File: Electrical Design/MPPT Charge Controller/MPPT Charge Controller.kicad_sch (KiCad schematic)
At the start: 0 parts

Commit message: Created BQ24650 symbol and footprint
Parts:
- added U1: ~, MPPT Charge Controller Footprint Library:VQFN-16_EP_3.5x3.5_Pitch0.5mm, symbol MPPT Charge Controller Symbol Library:BQ24650
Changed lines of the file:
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@@
 	(generator_version "8.0")
 	(paper "A4")
+	(symbol
+		(lib_id "MPPT Charge Controller Symbol Library:BQ24650")
+		(at 96.52 81.28 0)
+		(unit 1)
+		(exclude_from_sim no)
+		(in_bom yes)
+		(on_board yes)
+		(dnp no)
+		(fields_autoplaced yes)
+		(property "Reference" "U1"
+			(at 96.52 57.15 0)
+			(effects
+				(font
+					(size 1.27 1.27)
+				)
+			)
+		)
+		(property "Value" "~"
+			(at 96.52 59.69 0)
+			(effects
+				(font
+					(size 1.27 1.27)
+				)
+			)
+		)
+		(property "Footprint" "MPPT Charge Controller Footprint Library:VQFN-16_EP_3.5x3.5_Pitch0.5mm"
+			(at 96.52 58.928 0)
+			(effects
+				(font
+					(size 1.27 1.27)
+				)
+				(hide yes)
+			)
+		)
+		(property "Datasheet" ""
+			(at 96.52 81.28 0)
+			(effects
+				(font
+					(size 1.27 1.27)
+				)
+				(hide yes)
+			)
+		)
+		(property "Description" ""
+			(at 96.52 81.28 0)
+			(effects
+				(font
+					(size 1.27 1.27)
+				)
+				(hide yes)
+			)
+		)
+		(pin "14"
+		)
+		(pin "11"
+		)
+		(pin "8"
+		)
+		(pin "13"
+		)
+		(pin "1"
+		)
+		(pin "10"
+		)
+		(pin "12"
+		)
+		(pin "16"
+		)
+		(pin "2"
+		)
+		(pin "15"
+		)
+		(pin "3"
+		)
+		(pin "4"
+		)
+		(pin "5"
+		)
+		(pin "6"
+		)
+		(pin "7"
+		)
+		(pin "9"
+		)
+		(instances
+			(project "MPPT Charge Controller"
+				(path "/6fccb5b0-46ff-4014-9169-aa61e4064f3f"
+					(reference "U1")
+					(unit 1)
+				)
+			)
+		)
+	)
 	(sheet_instances
 		(path "/"

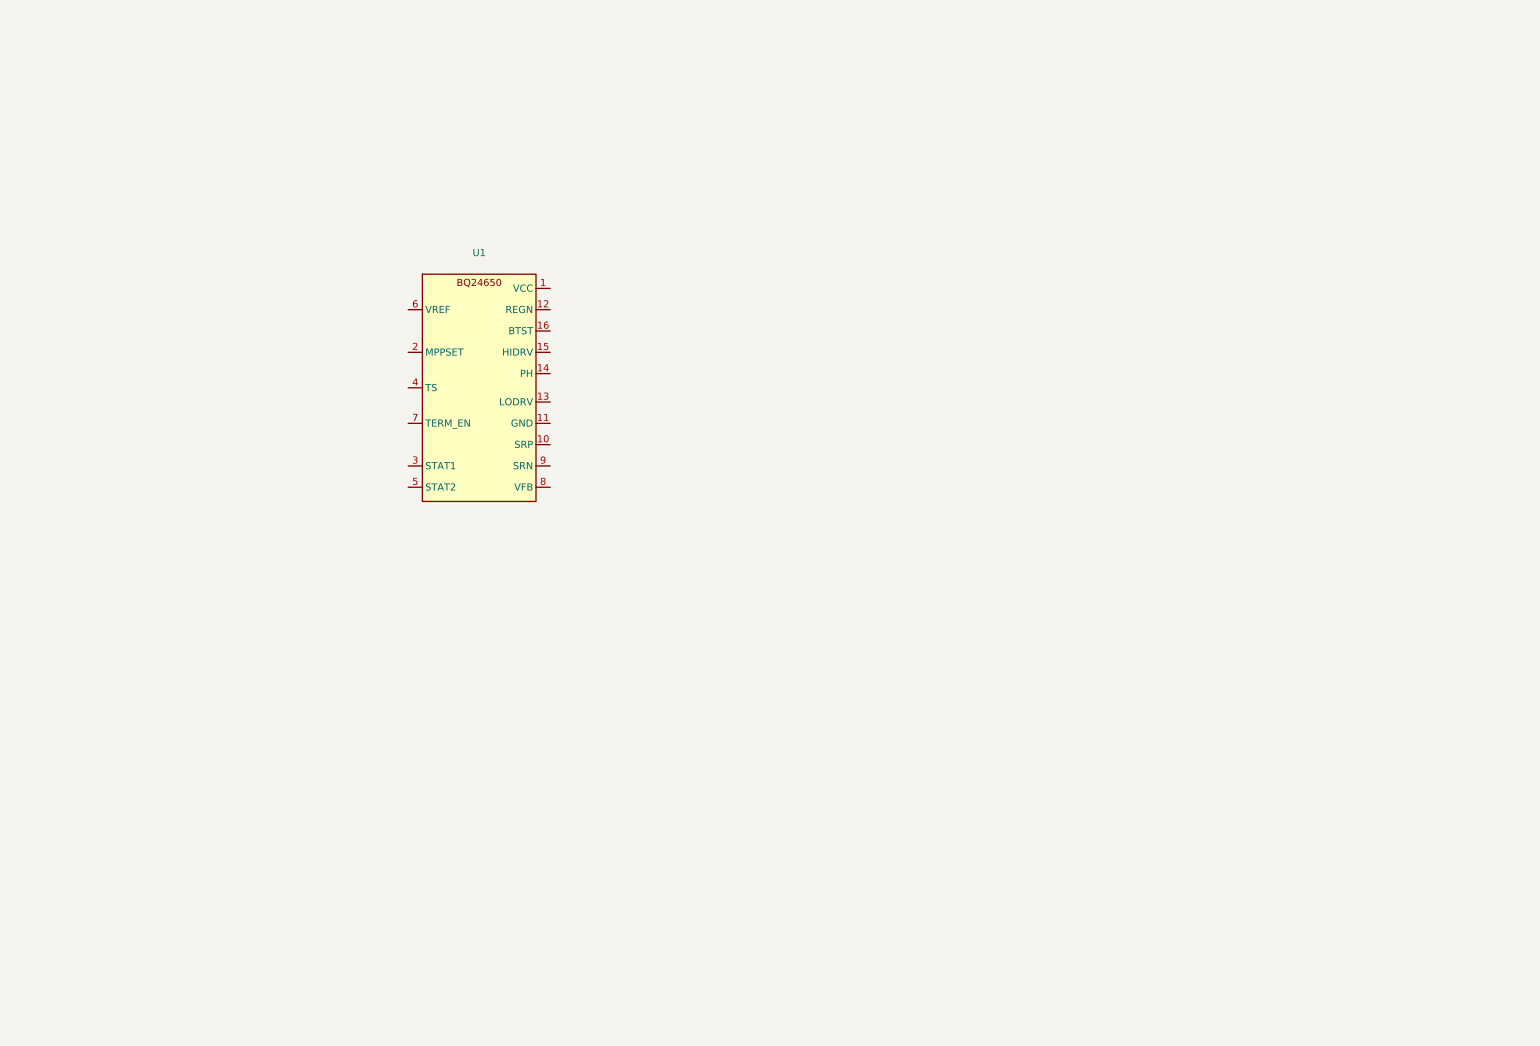
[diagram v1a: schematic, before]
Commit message: Added circuitry to schematic
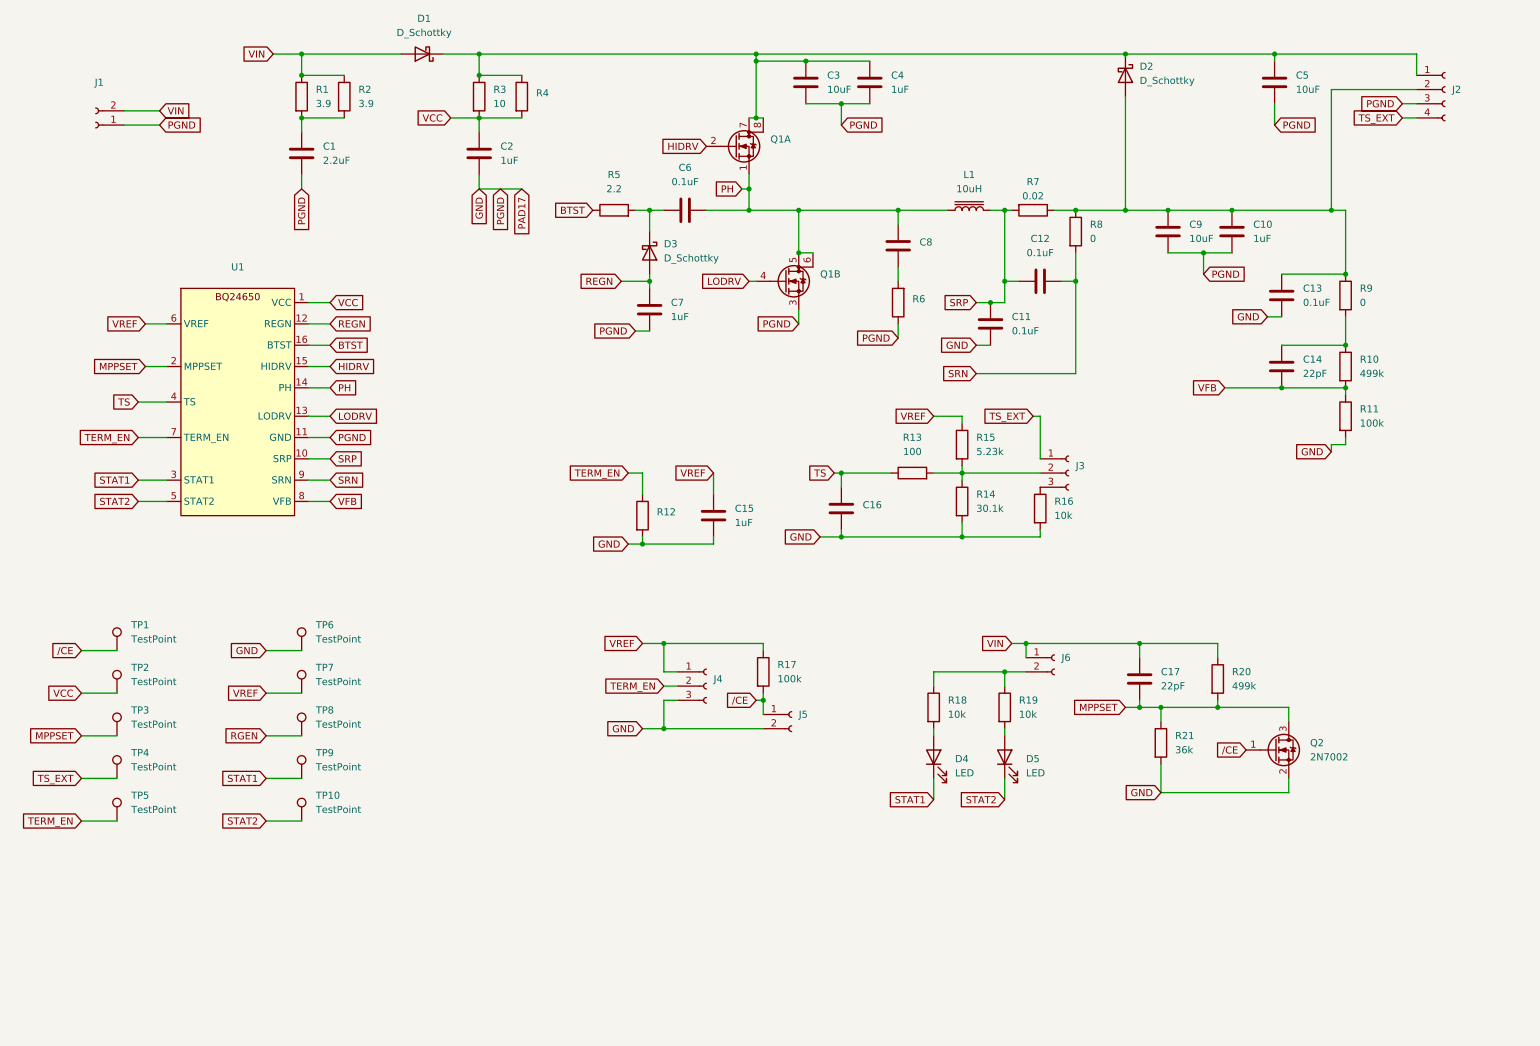
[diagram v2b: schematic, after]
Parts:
- added C1: 2.2uF, symbol Device:C
- added C10, C15, C2, C4, C7: 1uF, symbol Device:C
- added C11, C12, C13, C6: 0.1uF, symbol Device:C
- added C14, C17: 22pF, symbol Device:C
- added C16, C8: ~, symbol Device:C
- added C3, C5, C9: 10uF, symbol Device:C
- added D1, D2, D3: D_Schottky, symbol Device:D_Schottky
- added D4, D5: LED, symbol Device:LED
- added J1, J5, J6: Conn_01x02_Socket, symbol Connector:Conn_01x02_Socket
- added J2: Conn_01x04_Socket, symbol Connector:Conn_01x04_Socket
- added J3, J4: Conn_01x03_Socket, symbol Connector:Conn_01x03_Socket
- added L1: 10uH, symbol Device:L_Iron
- added Q1: Q_Dual_NMOS_S1G1S2G2D2D2D1D1, symbol Device:Q_Dual_NMOS_S1G1S2G2D2D2D1D1
- added Q2: 2N7002, Package_TO_SOT_SMD:SOT-23, symbol Transistor_FET:2N7002
- added R1, R2: 3.9, symbol Device:R
- added R10, R20: 499k, symbol Device:R
- added R11, R17: 100k, symbol Device:R
- added R12, R4, R6: ~, symbol Device:R
- added R13: 100, symbol Device:R
- added R14: 30.1k, symbol Device:R
- added R15: 5.23k, symbol Device:R
- added R16, R18, R19: 10k, symbol Device:R
- added R21: 36k, symbol Device:R
- added R3: 10, symbol Device:R
- added R5: 2.2, symbol Device:R
- added R7: 0.02, symbol Device:R
- added R8, R9: 0, symbol Device:R
- added TP1, TP10, TP2, TP3, TP4, TP5, TP6, TP7, TP8, TP9: TestPoint, symbol Connector:TestPoint
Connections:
- net VCC: now reaches U1.1 (VCC)
- net VCC: now also C2.1, R3.2, R4.2, TP2.1
- net SRP: now reaches U1.10 (SRP)
- net SRP: now also C11.2, C12.2, L1.2, R7.2
- net GND: now reaches U1.11 (GND)
- net GND: now also C1.2, C10.2, C11.1, C13.1, C15.2, C16.2, C2.2, C3.2, C4.2, C5.2, C7.1, C9.2, J1.1 (Pin_1), J2.3 (Pin_3), J4.3 (Pin_3), J5.2 (Pin_2), Q1.3 (S), Q2.2 (S), R11.2, R12.2, R14.2, R16.2, R21.2, R6.1, TP6.1
- net REGN: now reaches U1.12 (REGN)
- net REGN: now also C7.2, D3.2 (A)
- net LODRV: now reaches U1.13 (LODRV)
- net LODRV: now also Q1.4 (G)
- net PH: now reaches U1.14 (PH)
- net PH: now also C6.2, C8.1, L1.1, Q1.1 (S), Q1.5 (D), Q1.6 (D)
- net HIDRV: now reaches U1.15 (HIDRV)
- net HIDRV: now also Q1.2 (G)
- net BTST: now reaches U1.16 (BTST)
- net BTST: now also R5.1
- net MPPSET: now reaches U1.2 (MPPSET)
- net MPPSET: now also C17.2, Q2.3 (D), R20.2, R21.1, TP3.1
- net STAT1: now reaches U1.3 (STAT1)
- net STAT1: now also D4.1 (K), TP9.1
- net TS: now reaches U1.4 (TS)
- net TS: now also C16.1, R13.1
- net STAT2: now reaches U1.5 (STAT2)
- net STAT2: now also D5.1 (K), TP10.1
- net VREF: now reaches U1.6 (VREF)
- net VREF: now also C15.1, J4.1 (Pin_1), R15.1, R17.1, TP7.1
- net TERM_EN: now reaches U1.7 (TERM_EN)
- net TERM_EN: now also J4.2 (Pin_2), R12.1, TP5.1
- net VFB: now reaches U1.8 (VFB)
- net VFB: now also C14.1, R10.2, R11.1
- net SRN: now reaches U1.9 (SRN)
- net SRN: now also C12.1, R8.2
- new net: J3.2 (Pin_2), R13.2, R14.1, R15.2
- new net: J6.2 (Pin_2), R18.1, R19.1
- new net: D4.2 (A), R18.2
- new net: C6.1, D3.1 (K), R5.2
- new net: J3.3 (Pin_3), R16.1
- new net: C10.1, C13.2, C9.1, D2.2 (A), J2.2 (Pin_2), R7.1, R8.1, R9.1
- new net: C3.1, C4.1, C5.1, D1.1 (K), D2.1 (K), J2.1 (Pin_1), Q1.7 (D), Q1.8 (D), R3.1, R4.1
- new net: C8.2, R6.2
- new net: D5.2 (A), R19.2
- new net: C14.2, R10.1, R9.2
- new net: C1.1, R1.2, R2.2
- new net RGEN: TP8.1
- new net TS_EXT: J2.4 (Pin_4), J3.1 (Pin_1), TP4.1
- new net VIN: C17.1, D1.2 (A), J1.2 (Pin_2), J6.1 (Pin_1), R1.1, R2.1, R20.1
- new net /CE: J5.1 (Pin_1), Q2.1 (G), R17.2, TP1.1
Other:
- moved on the sheet: U1

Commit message: Rev .01
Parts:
- removed C10, C15, C4, C7: 1uF, symbol Device:C
- removed C16, C8: ~, symbol Device:C
- removed C17: 22pF, symbol Device:C
- removed C3, C5, C9: 10uF, symbol Device:C
- removed D2, D3: D_Schottky, symbol Device:D_Schottky
- removed D4: LED, symbol Device:LED
- removed J2: Conn_01x04_Socket, symbol Connector:Conn_01x04_Socket
- removed J3, J4: Conn_01x03_Socket, symbol Connector:Conn_01x03_Socket
- removed J5, J6: Conn_01x02_Socket, symbol Connector:Conn_01x02_Socket
- removed Q2: 2N7002, Package_TO_SOT_SMD:SOT-23, symbol Transistor_FET:2N7002
- removed R12, R6: ~, symbol Device:R
- removed R13: 100, symbol Device:R
- removed R14: 30.1k, symbol Device:R
- removed R15: 5.23k, symbol Device:R
- removed R16, R18: 10k, symbol Device:R
- removed R17: 100k, symbol Device:R
- removed R20: 499k, symbol Device:R
- removed R21: 36k, symbol Device:R
- removed R5: 2.2, symbol Device:R
- removed R8, R9: 0, symbol Device:R
- added A1: Adafruit_Feather_HUZZAH32_ESP32, Module:Adafruit_Feather, symbol MCU_Module:Adafruit_Feather_HUZZAH32_ESP32
- added C10: 22pF, Capacitor_SMD:C_0603_1608Metric, symbol Device:C_Small
- added C3, C4: 1uF, Capacitor_SMD:C_0603_1608Metric, symbol Device:C_Small
- added C5, C7: 0.1uF, Capacitor_SMD:C_0603_1608Metric, symbol Device:C_Small
- added C8: 10uF, Capacitor_SMD:C_1206_3216Metric, symbol Device:C_Small
- added C9: 4.7uF, Capacitor_SMD:C_0805_2012Metric, symbol Device:C_Small
- added D2: BAT54C, Package_TO_SOT_SMD:SOT-23, symbol Diode:BAT54C
- added D4: GREEN, LED_SMD:LED_0603_1608Metric, symbol Device:LED_Small_Filled
- added J2, J3: Conn_01x02_Socket, TerminalBlock:TerminalBlock_bornier-2_P5.08mm, symbol Connector:Screw_Terminal_01x02
- added L2: 4.7uH, Inductor_SMD:L_Vishay_IFSC-1515AH_4x4x1.8mm, symbol Device:L
- added NT1, NT2, NT3, NT4: ~, NetTie:NetTie-2_SMD_Pad0.5mm, symbol Device:NetTie_2
- added Q2: Q_Dual_NMOS_S1G1S2G2D2D2D1D1, Package_SO:PowerPAK_SO-8_Dual, symbol Device:Q_Dual_NMOS_S1G1S2G2D2D2D1D1
- added Q3: 2N7002, Package_TO_SOT_SMD:SOT-23, symbol Transistor_FET:2N7002
- added R11, R14: 100k, Resistor_SMD:R_0603_1608Metric, symbol Device:R_Small_US
- added R12, R15: 499k, Resistor_SMD:R_0603_1608Metric, symbol Device:R_Small_US
- added R13: 68k, Resistor_SMD:R_0603_1608Metric, symbol Device:R_Small_US
- added R16: 150k, Resistor_SMD:R_0603_1608Metric, symbol Device:R_Small_US
- added R6: 10, Resistor_SMD:R_0603_1608Metric, symbol Device:R_Small_US
- added R8: 10k, Resistor_SMD:R_0603_1608Metric, symbol Device:R_Small_US
- added R9: 5.23k, Resistor_SMD:R_0603_1608Metric, symbol Device:R_Small_US
- added TP11, TP12, TP13: TestPoint, TestPoint:TestPoint_Pad_D1.0mm, symbol Connector:TestPoint
- added TP14, TP15: TestPoint, TestPoint:TestPoint_Loop_D2.60mm_Drill1.6mm_Beaded, symbol Connector:TestPoint
- added U2: AP63203WU, Package_TO_SOT_SMD:TSOT-23-6, symbol Regulator_Switching:AP63203WU
- added U3: ACS712xLCTR-05B, Package_SO:SOIC-8_3.9x4.9mm_P1.27mm, symbol Sensor_Current:ACS712xLCTR-05B
- added U4: ACS712, Package_SO:SOIC-8_3.9x4.9mm_P1.27mm, symbol Sensor_Current:ACS712xLCTR-05B
- C1: footprint (none) -> Capacitor_SMD:C_1210_3225Metric; symbol Device:C -> Device:C_Small
- C11: value 0.1uF -> 10uF; footprint (none) -> Capacitor_SMD:C_0603_1608Metric
- C12: footprint (none) -> Capacitor_SMD:C_0603_1608Metric
- C13: value 0.1uF -> 22uF; footprint (none) -> Capacitor_SMD:C_0603_1608Metric
- C14: value 22pF -> 22uF; footprint (none) -> Capacitor_SMD:C_0603_1608Metric
- C2: footprint (none) -> Capacitor_SMD:C_0603_1608Metric; symbol Device:C -> Device:C_Small
- C6: value 0.1uF -> 10uF; footprint (none) -> Capacitor_SMD:C_1206_3216Metric; symbol Device:C -> Device:C_Small
- D1: value D_Schottky -> PDS1040; footprint (none) -> Diode_SMD:D_PowerDI-5; symbol Device:D_Schottky -> Device:D_Small
- D3: renamed from D5; value LED -> RED; footprint (none) -> LED_SMD:LED_0603_1608Metric; symbol Device:LED -> Device:LED_Small_Filled
- J1: footprint (none) -> TerminalBlock:TerminalBlock_bornier-2_P5.08mm; symbol Connector:Conn_01x02_Socket -> Connector:Screw_Terminal_01x02
- L1: footprint (none) -> MPPT Charge Controller Footprint Library:L_Vishay_6.9x6.5
- Q1: footprint (none) -> Package_SO:PowerPAK_SO-8_Dual
- R1: renamed from R11; footprint (none) -> Resistor_SMD:R_0603_1608Metric; symbol Device:R -> Device:R_Small_US
- R10: renamed from R2; value 3.9 -> 30.1k; footprint (none) -> Resistor_SMD:R_0603_1608Metric; symbol Device:R -> Device:R_Small_US
- R2: renamed from R10; footprint (none) -> Resistor_SMD:R_0603_1608Metric; symbol Device:R -> Device:R_Small_US
- R3: value 10 -> 499k; footprint (none) -> Resistor_SMD:R_0603_1608Metric; symbol Device:R -> Device:R_Small_US
- R4: value ~ -> 36k; footprint (none) -> Resistor_SMD:R_0603_1608Metric; symbol Device:R -> Device:R_Small_US
- R5: renamed from R1; value 3.9 -> 2; footprint (none) -> Resistor_SMD:R_2512_6332Metric; symbol Device:R -> Device:R_Small_US
- R7: renamed from R19; footprint (none) -> Resistor_SMD:R_0603_1608Metric; symbol Device:R -> Device:R_Small_US
- RSR1: renamed from R7; footprint (none) -> Resistor_SMD:R_1206_3216Metric; symbol Device:R -> Device:R_Small_US
- TP1, TP10, TP2, TP3, TP4, TP5, TP6, TP7, TP8, TP9: footprint (none) -> TestPoint:TestPoint_Pad_D1.0mm
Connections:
- net REGN is gone; now on net RGEN: U1.12 (REGN)
- net TS_EXT is gone; now on net TS: TP4.1
- net /CE is gone; now on net VCC: TP1.1
- net BTST: now also TP9.1, C5.2, D2.3
- net GND: now also C13.2, C14.2, C6.1, A1.4 (GND), C4.2, C8.1, C9.1, J2.1 (Pin_1), NT1.2, NT2.2, NT3.2, NT4.2, Q2.1 (S), R13.2, R16.2, TP14.1, U2.4 (GND), U3.5 (GND), U4.5 (GND); no longer C13.1, C2.2, R1.2, TP6.1, U1.11 (GND)
- net HIDRV: now also TP10.1
- net LODRV: now also TP11.1
- net MPPSET: now also R3.2, R4.1, Q3.3 (D)
- net PH: now also C5.1, TP12.1; no longer C6.2
- net RGEN: now also C4.1, D2.2
- net STAT1: now also D3.1 (K), TP6.1, A1.19 (D5); no longer TP9.1
- net STAT2: now also TP7.1, A1.20 (D6), D4.1 (K); no longer D3.1 (K), TP10.1
- net TS: now also R10.1, R9.2
- net VCC: now also R6.2; no longer R3.2, R4.2, TP2.1
- net VFB: now also TP5.1, C10.1; no longer C14.1
- net VIN: now also C11.2, R3.1, U2.2 (EN), U2.3 (IN), U3.3 (IP-), U3.4 (IP-); no longer J1.2 (Pin_2), R10.1
- net VREF: now also R7.1, TP2.1, U1.7 (TERM_EN), C3.1, R8.1, R9.1; no longer TP7.1
- net at RSR1.1: now also R2.1, U1.9 (SRN), C10.2, C7.2, C8.2, C9.2, U4.1 (IP+), U4.2 (IP+); no longer C13.2
- net at D1.1 (K), Q1.7 (D), Q1.8 (D): now also C6.2, R6.1; no longer R3.1, R4.1
- net at C1.1, R5.2: no longer R10.2
- net SRN: no longer names the net of C12.1
- net SRN: now also L2.1, U2.5 (SW); no longer U1.9 (SRN)
- net SRP: no longer names the net of L1.2, RSR1.2, U1.10 (SRP)
- net SRP: now also C7.1; no longer C11.2, C12.2
- removed net TERM_EN: TP5.1, U1.7 (TERM_EN)
- new net: J2.2 (Pin_2), J3.2 (Pin_2), R15.1, U4.3 (IP-), U4.4 (IP-)
- new net: C12.2, U2.6 (BST)
- new net: R11.1, U4.6 (FILTER)
- new net: D4.2 (A), R8.2
- new net: R14.1, U3.6 (FILTER)
- new net: J3.1 (Pin_1), Q2.7 (D), Q2.8 (D)
- new net: Q2.5 (D), Q2.6 (D)
- new net +3.3V: A1.2 (3V3), C13.1, C14.1, L2.2, R11.2, R14.2, U2.1 (FB), U3.8 (VCC), U4.8 (VCC)
- new net Battery Current: A1.8 (I39/A3), U4.7 (VIOUT)
- new net Battery Voltage: A1.7 (I34/A2), R15.2, R16.1
- new net Input: J1.2 (Pin_2), R12.1, TP15.1, U3.1 (IP+), U3.2 (IP+)
- new net Load Enable: A1.23 (D11), Q2.2 (G)
- new net PWR GND: C2.2, C3.2, NT1.1, NT2.1, NT3.1, NT4.1, Q3.2 (S), R1.2, R10.2, R4.2, U1.11 (GND), U1.17 (Thermal_Pad)
- new net SD_CS: A1.22 (D10)
- new net Solar Current: A1.6 (DAC1/A1), U3.7 (VIOUT)
- new net Solar Voltage: A1.5 (DAC2/A0), R12.2, R13.1
- new net ~{Charge EN}: A1.21 (D9), Q3.1 (G), TP13.1
- no-connect marks 0 -> 20
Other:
- note added: "12V Battery"
- note added: "12V Load"
- note added: "5V-28V Solar input"
- note added: "connected to GND through board vias"
- moved on the sheet: C1, C2, C6, D1, L1, Q1A, Q1B, TP1, TP10, TP2, TP3, TP4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
